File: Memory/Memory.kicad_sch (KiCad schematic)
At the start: 13 parts, among them U1 62256, U2 6264, U3 6264, U4 28C64, U5 74LS139

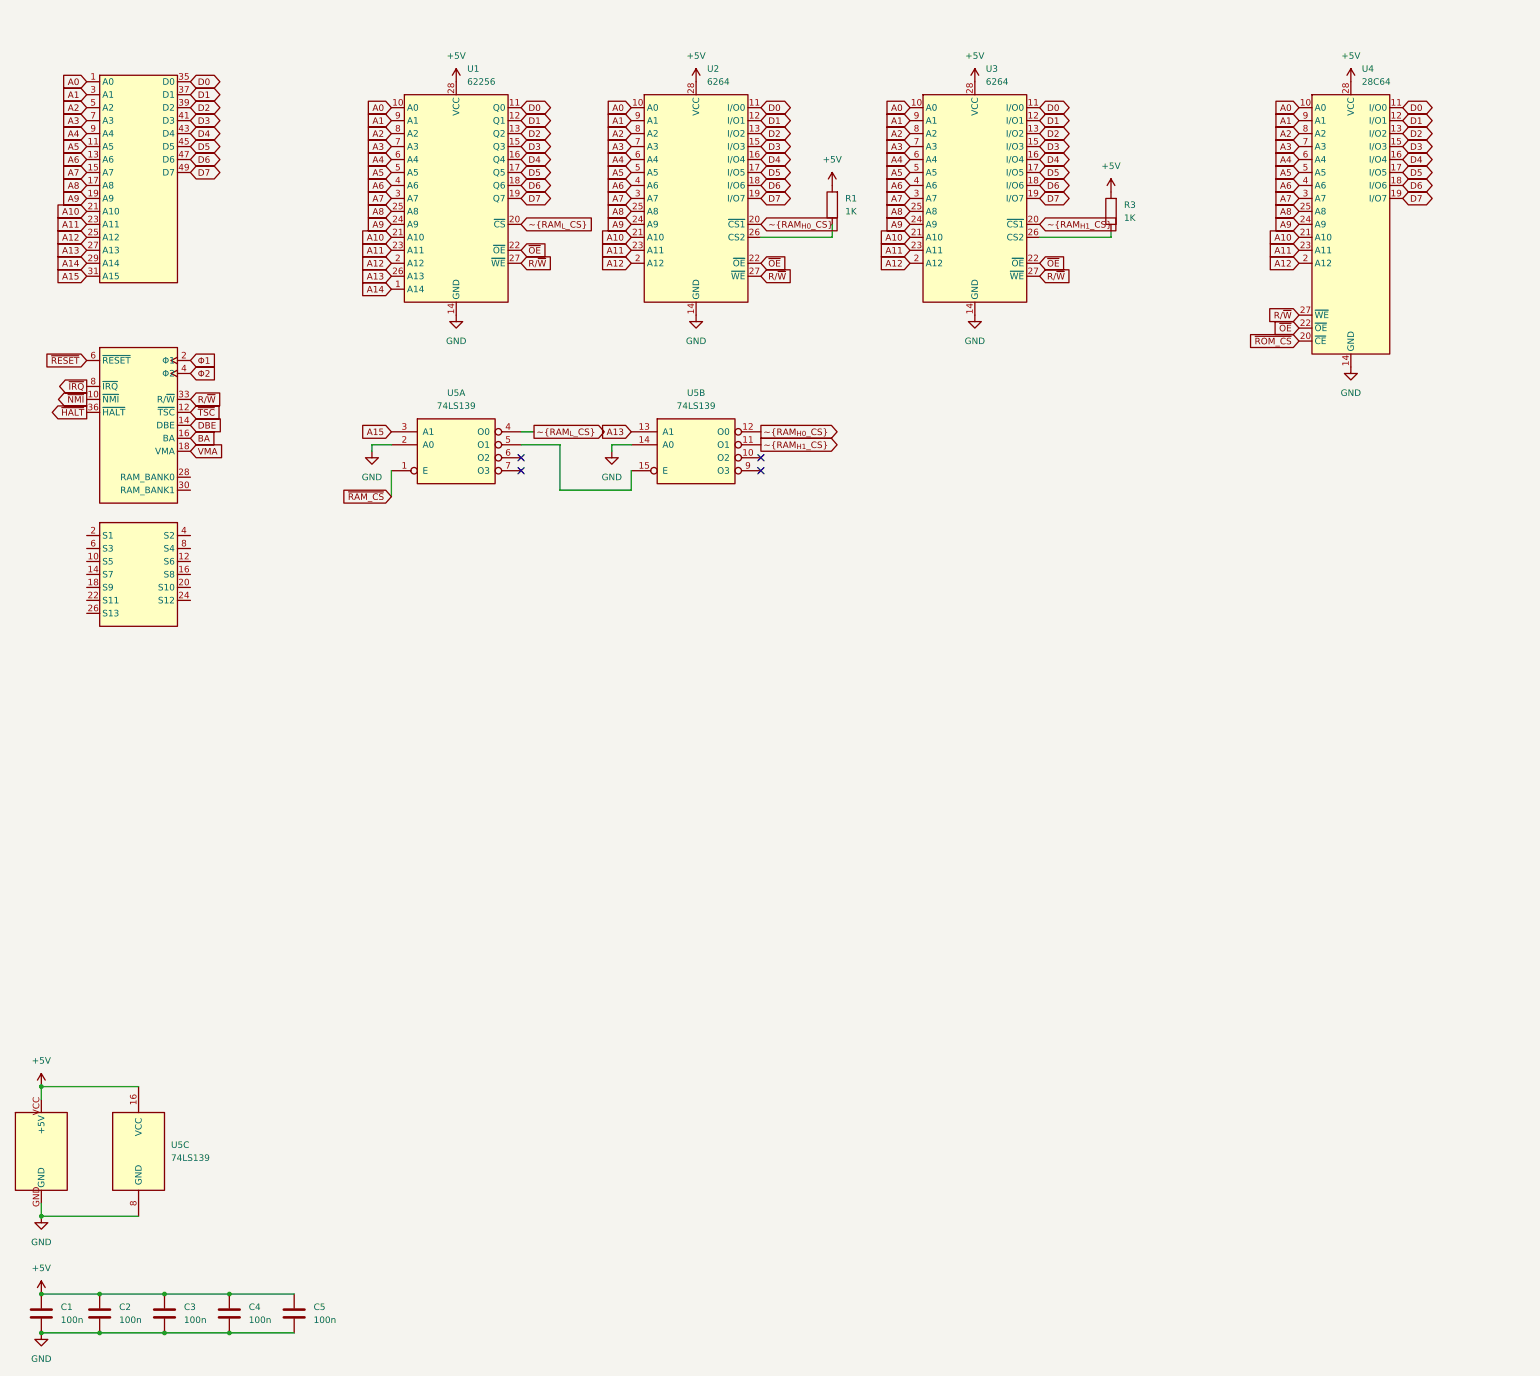
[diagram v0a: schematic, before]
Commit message: outputs to terminal/log file
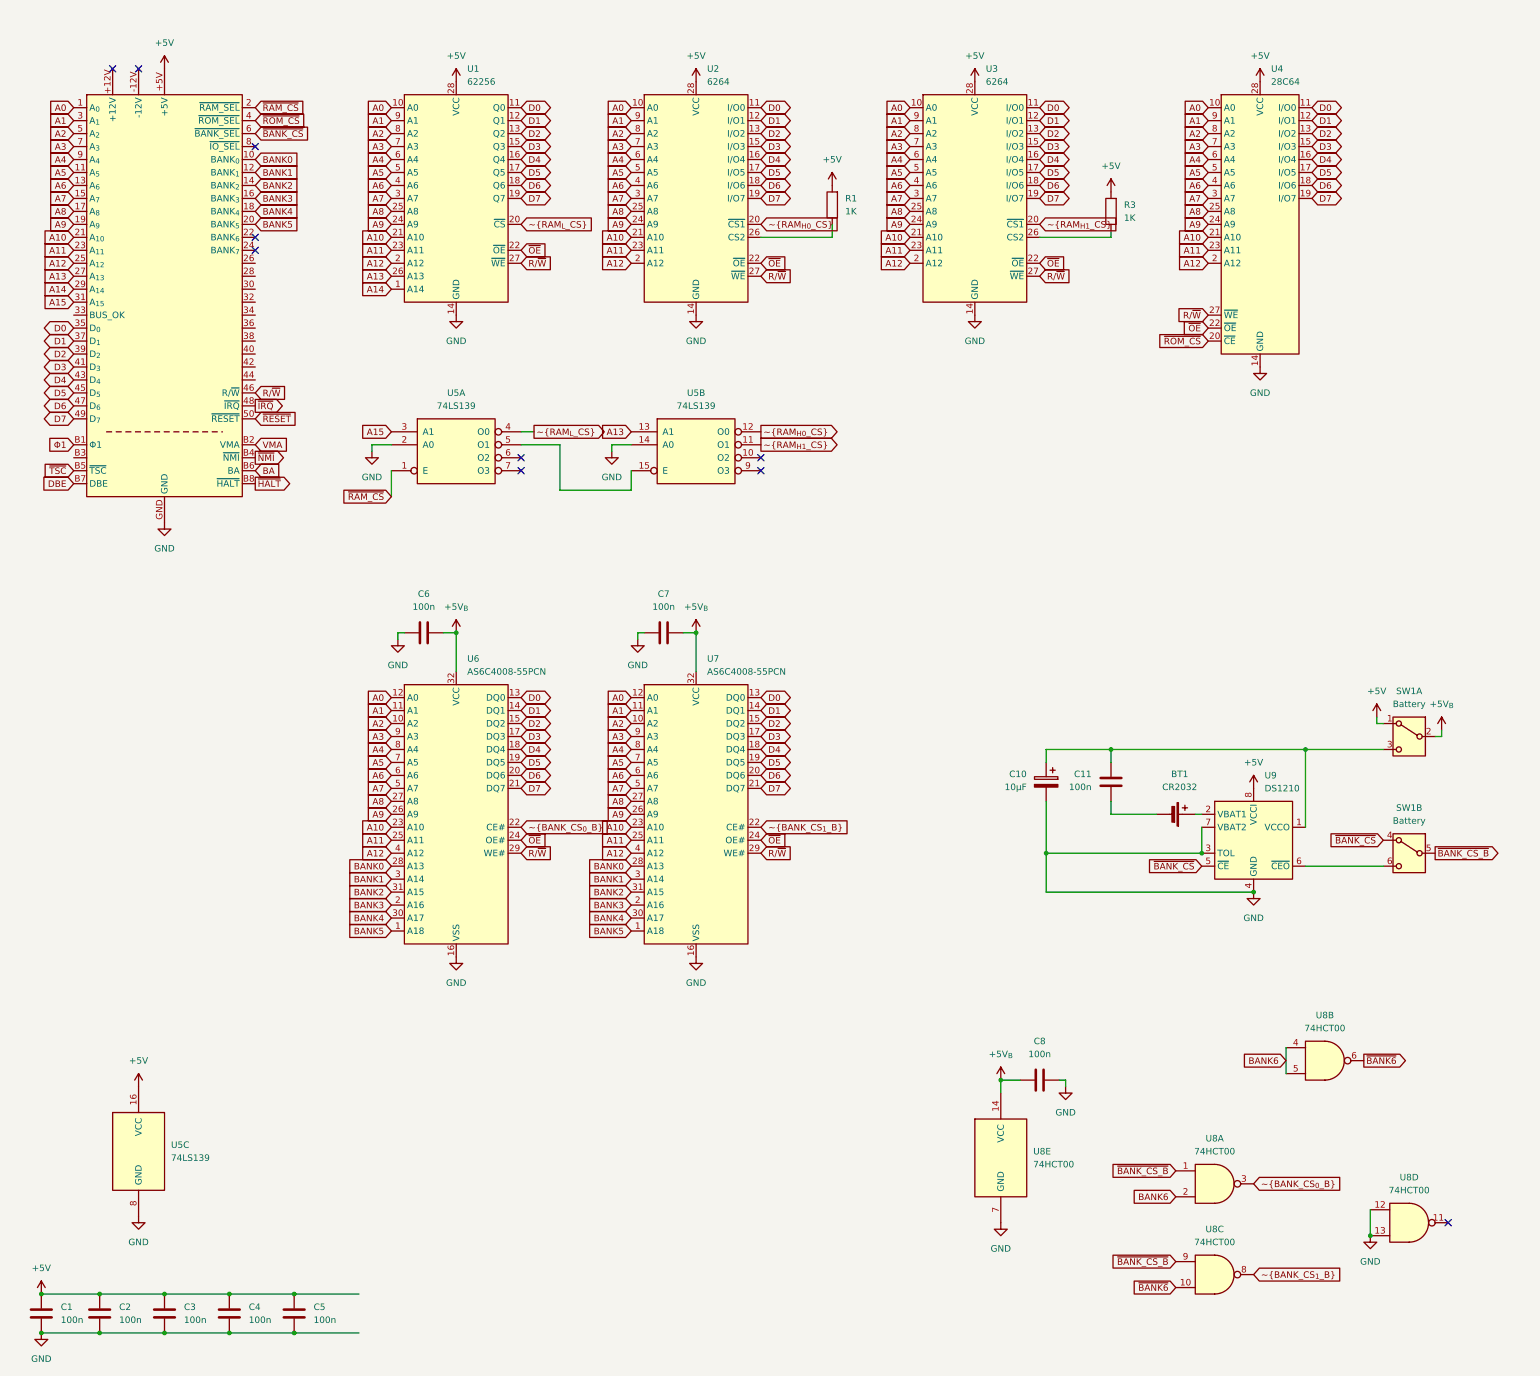
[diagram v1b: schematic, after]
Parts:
- removed unit 4 of BRD1
- removed unit 3 of BRD1
- removed unit 2 of BRD1
- added BT1: CR2032, Battery:BatteryHolder_MYOUNG_BS-07-A1BJ001_CR2032, symbol Device:Battery_Cell
- added C10: 10µF, Capacitor_THT:CP_Radial_D5.0mm_P2.50mm, symbol Device:C_Polarized
- added C11, C6, C7, C8: 100n, Capacitor_THT:C_Disc_D3.0mm_W1.6mm_P2.50mm, symbol Device:C
- added SW1: Battery, Button_Switch_THT:SW_CK_JS202011CQN_DPDT_Straight, symbol Switch:SW_DPDT_x2
- added U6, U7: AS6C4008-55PCN, Package_DIP:DIP-32_W15.24mm, symbol Memory_RAM:AS6C4008-55PCN
- added U8: 74HCT00, Package_DIP:DIP-14_W7.62mm, symbol 74xx:74LS00
- added U9: DS1210, Package_DIP:DIP-8_W7.62mm_Socket, symbol Power_Management:DS1210
- BRD1: symbol 0-Symbols:Card -> 0-Symbols:Buss
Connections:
- net +5V: now also BRD1.+5V, SW1.1 (A), U9.8 (VCCI)
- net A0: now also U6.12 (A0), U7.12 (A0)
- net A1: now also U6.11 (A1), U7.11 (A1)
- net A10: now also U6.23 (A10), U7.23 (A10)
- net A11: now also U6.25 (A11), U7.25 (A11)
- net A12: now also U6.4 (A12), U7.4 (A12)
- net A2: now also U6.10 (A2), U7.10 (A2)
- net A3: now also U6.9 (A3), U7.9 (A3)
- net A4: now also U6.8 (A4), U7.8 (A4)
- net A5: now also U6.7 (A5), U7.7 (A5)
- net A6: now also U6.6 (A6), U7.6 (A6)
- net A7: now also U6.5 (A7), U7.5 (A7)
- net A8: now also U6.27 (A8), U7.27 (A8)
- net A9: now also U6.26 (A9), U7.26 (A9)
- net BA: now also BRD1.B6 (BA)
- net D0: now also U6.13 (DQ0), U7.13 (DQ0)
- net D1: now also U6.14 (DQ1), U7.14 (DQ1)
- net D2: now also U6.15 (DQ2), U7.15 (DQ2)
- net D3: now also U6.17 (DQ3), U7.17 (DQ3)
- net D4: now also U6.18 (DQ4), U7.18 (DQ4)
- net D5: now also U6.19 (DQ5), U7.19 (DQ5)
- net D6: now also U6.20 (DQ6), U7.20 (DQ6)
- net D7: now also U6.21 (DQ7), U7.21 (DQ7)
- net DBE: now also BRD1.B7 (DBE)
- net GND: now also BRD1.GND, C10.2, C6.2, C7.2, C8.1, U6.16 (VSS), U7.16 (VSS), U8.12, U8.13, U8.7 (GND), U9.3 (TOL), U9.4 (GND), U9.7 (VBAT2)
- net R/~{W}: now also BRD1.46 (R/~{W}), U6.29 (WE#), U7.29 (WE#)
- net VMA: now also BRD1.B2 (VMA)
- net ~{HALT}: now also BRD1.B8 (~{HALT})
- net ~{IRQ}: now also BRD1.48 (~{IRQ})
- net ~{NMI}: now also BRD1.B4 (~{NMI})
- net ~{OE}: now also U6.24 (OE#), U7.24 (OE#)
- net ~{RAM_CS}: now also BRD1.2 (~{RAM_SEL})
- net ~{RESET}: now also BRD1.50 (~{RESET})
- net ~{ROM_CS}: now also BRD1.4 (~{ROM_SEL})
- net ~{TSC}: now also BRD1.B5 (~{TSC})
- net Φ1: now also BRD1.B1 (Φ1)
- new net: C10.1, C11.2, SW1.3 (C), U9.1 (VCCO)
- new net: BT1.1 (+), U9.2 (VBAT1)
- new net: SW1.6 (C), U9.6 (~{CEO})
- new net: BT1.2 (-), C11.1
- new net +5V_{B}: C6.1, C7.1, C8.2, SW1.2 (B), U6.32 (VCC), U7.32 (VCC), U8.14 (VCC)
- new net BANK0: BRD1.10 (BANK_{0}), U6.28 (A13), U7.28 (A13)
- new net BANK1: BRD1.12 (BANK_{1}), U6.3 (A14), U7.3 (A14)
- new net BANK2: BRD1.14 (BANK_{2}), U6.31 (A15), U7.31 (A15)
- new net BANK3: BRD1.16 (BANK_{3}), U6.2 (A16), U7.2 (A16)
- new net BANK4: BRD1.18 (BANK_{4}), U6.30 (A17), U7.30 (A17)
- new net BANK5: BRD1.20 (BANK_{5}), U6.1 (A18), U7.1 (A18)
- new net BANK6: U8.2, U8.4, U8.5
- new net ~{BANK6}: U8.10, U8.6
- new net ~{BANK_CS_B}: SW1.5 (B), U8.1, U8.9
- new net ~{BANK_CS_{0}_B}: U6.22 (CE#), U8.3
- new net ~{BANK_CS_{1}_B}: U7.22 (CE#), U8.8
- new net ~{BANK_CS}: BRD1.6 (~{BANK_SEL}), SW1.4 (A), U9.5 (~{CE})
- no-connect marks 4 -> 10
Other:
- moved on the sheet: U4

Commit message: a bunch of stuff
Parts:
- removed BRD1: Card, 0-Footprints:Card, symbol 0-Symbols:Buss
- removed BT1: CR2032, Battery:BatteryHolder_MYOUNG_BS-07-A1BJ001_CR2032, symbol Device:Battery_Cell
- removed C10: 10µF, Capacitor_THT:CP_Radial_D5.0mm_P2.50mm, symbol Device:C_Polarized
- removed C11, C6, C7, C8: 100n, Capacitor_THT:C_Disc_D3.0mm_W1.6mm_P2.50mm, symbol Device:C
- removed SW1: Battery, Button_Switch_THT:SW_CK_JS202011CQN_DPDT_Straight, symbol Switch:SW_DPDT_x2
- removed U6, U7: AS6C4008-55PCN, Package_DIP:DIP-32_W15.24mm, symbol Memory_RAM:AS6C4008-55PCN
- removed U8: 74HCT00, Package_DIP:DIP-14_W7.62mm, symbol 74xx:74LS00
- removed U9: DS1210, Package_DIP:DIP-8_W7.62mm_Socket, symbol Power_Management:DS1210
- added J1: Buss, symbol 0-Symbols:Buss
- U1: value 62256 -> FM1808
- U2, U3: value 6264 -> FM1608
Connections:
- net +5V: now also J1.P1 (+5V)
- net A0: now also J1.1 (A_{0})
- net A1: now also J1.3 (A_{1})
- net A10: now also J1.21 (A_{10})
- net A11: now also J1.23 (A_{11})
- net A12: now also J1.25 (A_{12})
- net A13: now also J1.27 (A_{13})
- net A14: now also J1.29 (A_{14})
- net A15: now also J1.31 (A_{15})
- net A2: now also J1.5 (A_{2})
- net A3: now also J1.7 (A_{3})
- net A4: now also J1.9 (A_{4})
- net A5: now also J1.11 (A_{5})
- net A6: now also J1.13 (A_{6})
- net A7: now also J1.15 (A_{7})
- net A8: now also J1.17 (A_{8})
- net A9: now also J1.19 (A_{9})
- net BA: now also J1.B6 (BA)
- net D0: now also J1.35 (D_{0})
- net D1: now also J1.37 (D_{1})
- net D2: now also J1.39 (D_{2})
- net D3: now also J1.41 (D_{3})
- net D4: now also J1.43 (D_{4})
- net D5: now also J1.45 (D_{5})
- net D6: now also J1.47 (D_{6})
- net D7: now also J1.49 (D_{7})
- net DBE: now also J1.B7 (DBE)
- net GND: now also J1.P2 (GND)
- net R/~{W}: now also J1.46 (R/~{W})
- net VMA: now also J1.B2 (VMA)
- net ~{HALT}: now also J1.B8 (~{HALT})
- net ~{IRQ}: now also J1.48 (~{IRQ})
- net ~{NMI}: now also J1.B4 (~{NMI})
- net ~{RAM_CS}: now also J1.2 (~{RAM_SEL})
- net ~{RESET}: now also J1.50 (~{RESET})
- net ~{ROM_CS}: now also J1.4 (~{ROM_SEL})
- net ~{TSC}: now also J1.B5 (~{TSC})
- net Φ1: now also J1.B1 (Φ1)
- new net BUS_OK: J1.33 (BUS_OK)
- new net Φ2: J1.B3 (Φ2)
- no-connect marks 10 -> 8
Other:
- moved on the sheet: U5C
